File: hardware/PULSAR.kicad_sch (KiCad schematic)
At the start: 7 parts, among them J1 Conn_01x20, U1 AP2112K-3.3, U2 SS49E, U3 CD74HC4067M, U4 ADS8688

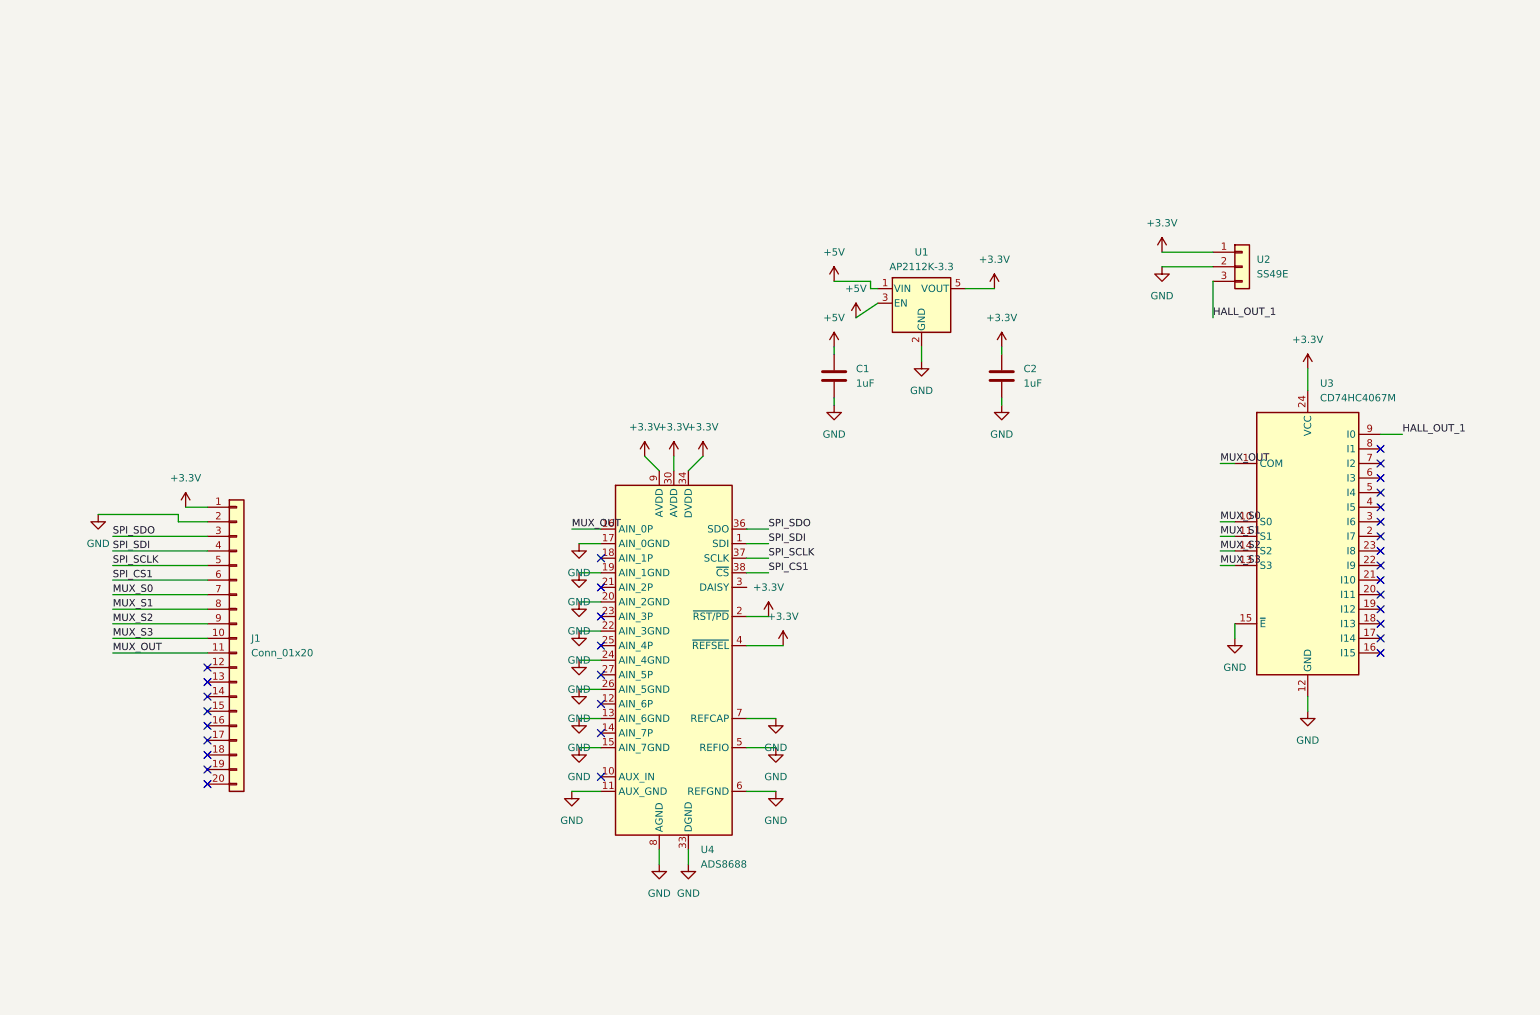
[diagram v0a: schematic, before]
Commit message: feat: add OLED SSD1306 connector with SPI signals
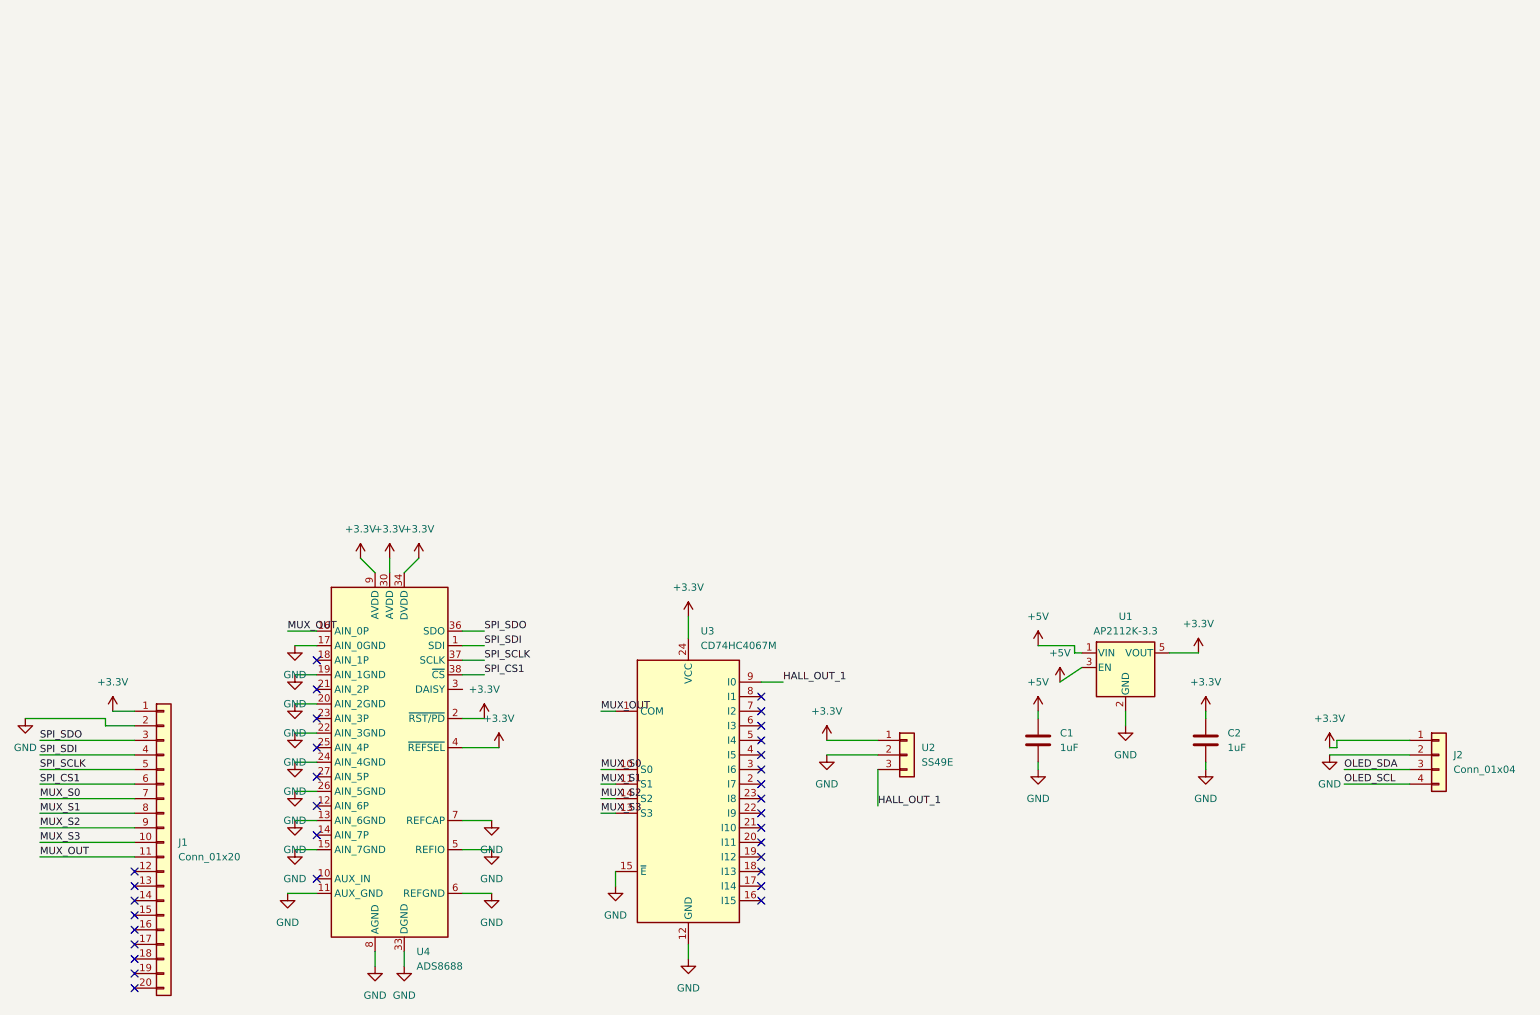
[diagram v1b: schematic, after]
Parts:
- added J2: Conn_01x04, symbol Connector_Generic:Conn_01x04
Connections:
- net +3.3V: now also J2.1 (Pin_1)
- net GND: now also J2.2 (Pin_2)
- new net OLED_SCL: J2.4 (Pin_4)
- new net OLED_SDA: J2.3 (Pin_3)
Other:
- moved on the sheet: C1, C2, J1, U1, U2, U3, U4

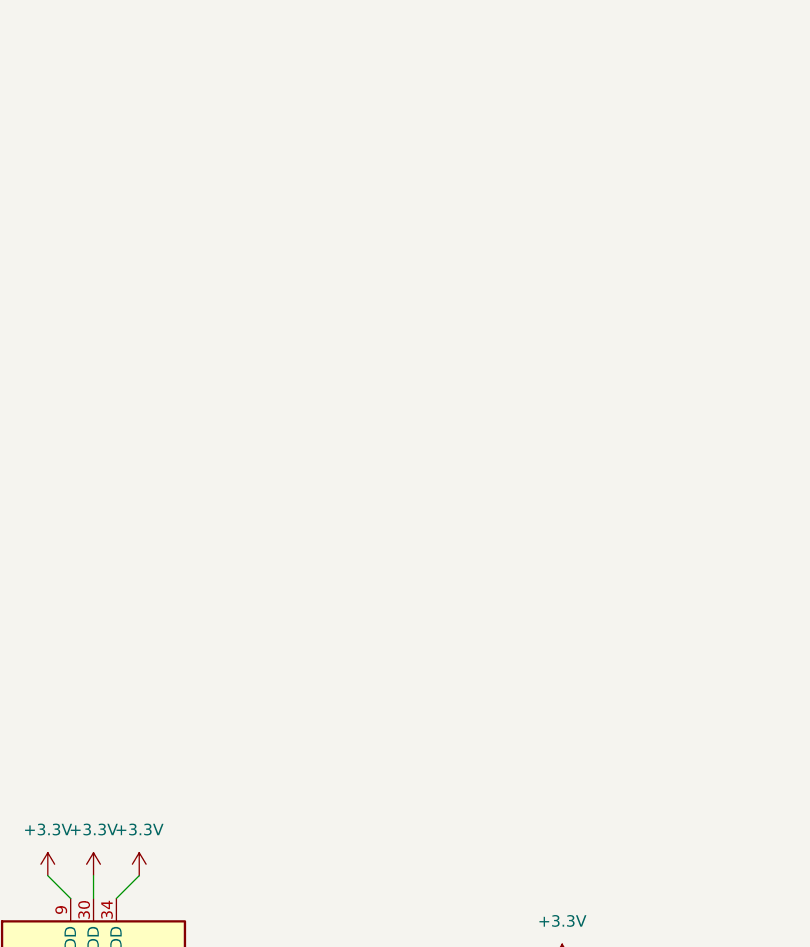
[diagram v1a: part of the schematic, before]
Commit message: feat: add USB-C connector with power and data signals
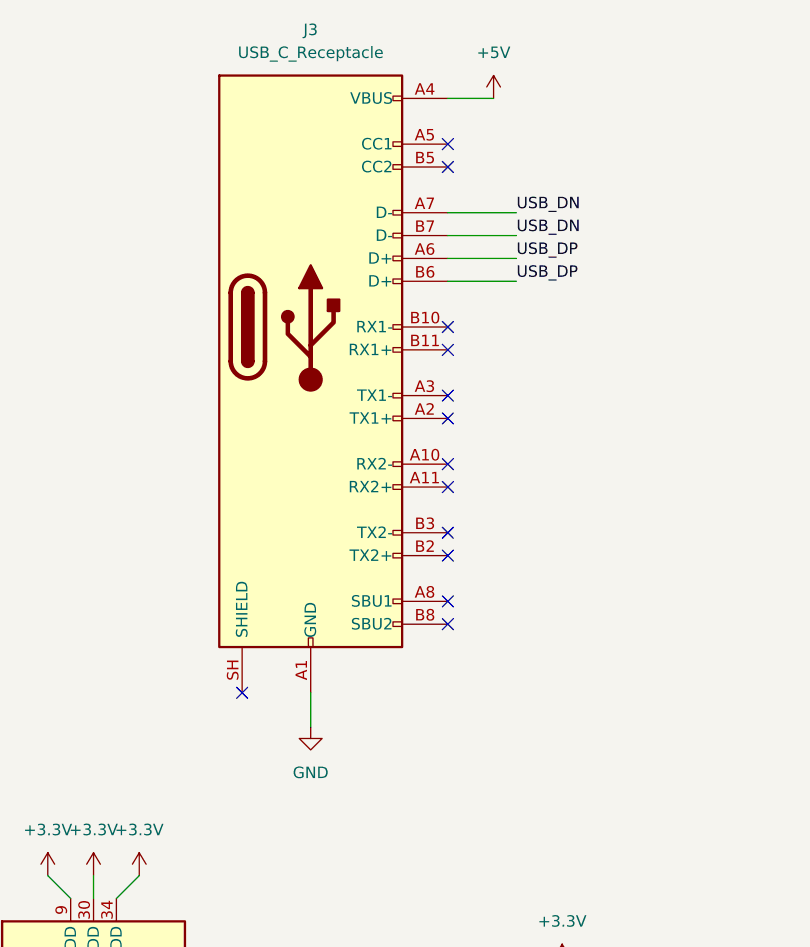
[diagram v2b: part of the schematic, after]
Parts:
- added J3: USB_C_Receptacle, symbol Connector:USB_C_Receptacle
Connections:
- net +5V: now also J3.A4 (VBUS), J3.A9 (VBUS), J3.B4 (VBUS), J3.B9 (VBUS)
- net GND: now also J3.A1 (GND), J3.A12 (GND), J3.B1 (GND), J3.B12 (GND)
- new net USB_DN: J3.A7 (D-), J3.B7 (D-)
- new net USB_DP: J3.A6 (D+), J3.B6 (D+)
- no-connect marks 32 -> 45

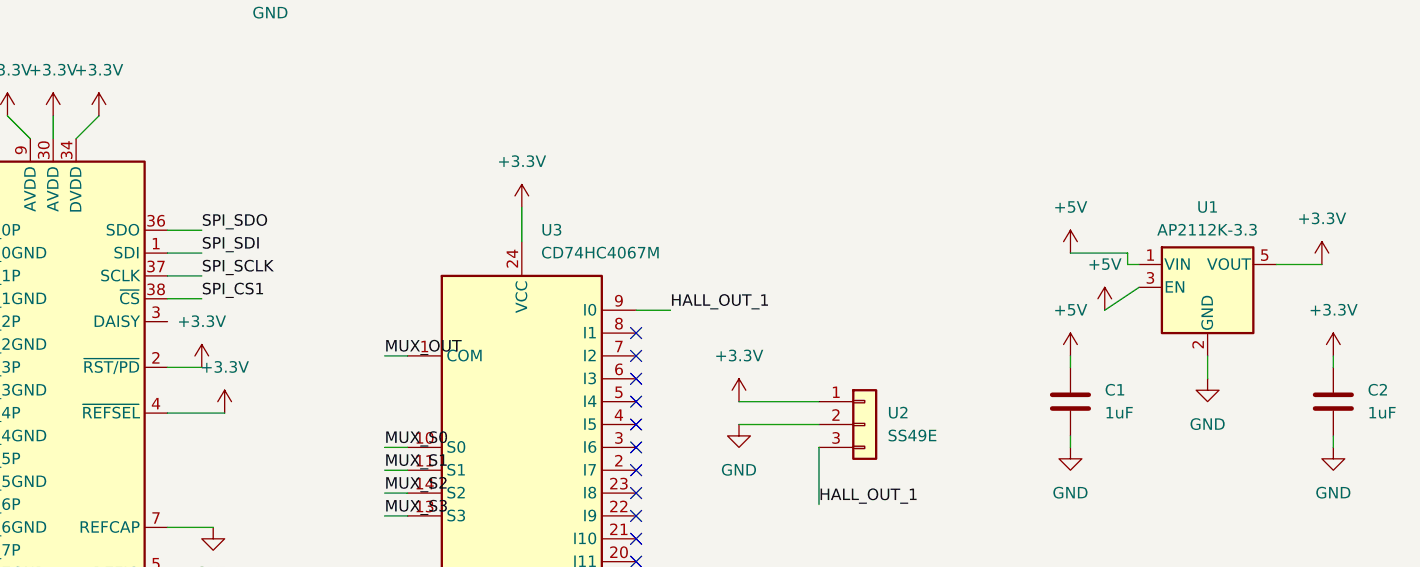
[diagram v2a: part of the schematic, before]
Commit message: fix: resolve ERC errors, add PWR_FLAG and DAISY no-connect
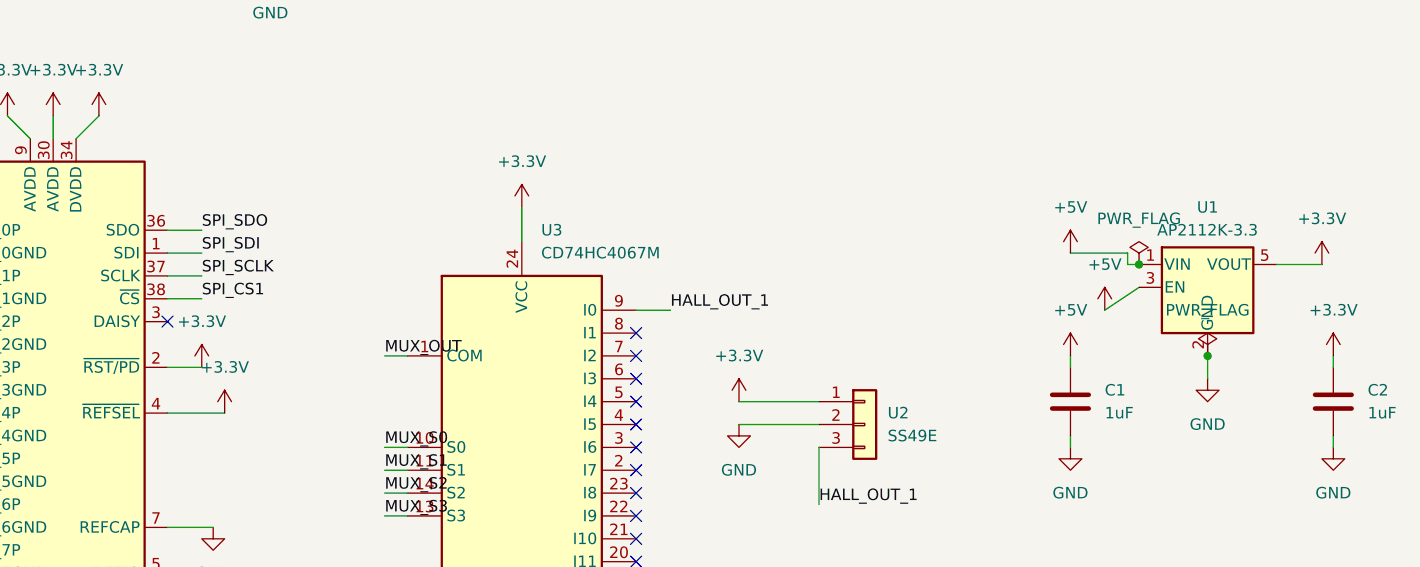
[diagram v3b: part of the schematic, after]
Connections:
- no-connect marks 45 -> 46
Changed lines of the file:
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@@
 	(generator_version "10.0")
 	(paper "A4")
+	(junction
+		(at 209.55 144.78)
+		(diameter 0)
+		(color 0 0 0 0)
+	)
+	(junction
+		(at 201.93 134.62)
+		(diameter 0)
+		(color 0 0 0 0)
+	)
 	(no_connect
 		(at 68.58 161.29)
@@
 	(no_connect
 		(at 146.05 144.78)
+	)
+	(no_connect
+		(at 93.98 140.97)
 	)
 	(no_connect
@@
 	)
 	(symbol
+		(lib_id "power:PWR_FLAG")
+		(at 209.55 144.78 0)
+		(unit 1)
+		(body_style 1)
+		(exclude_from_sim no)
+		(in_bom yes)
+		(on_board yes)
+		(in_pos_files yes)
+		(dnp no)
+		(fields_autoplaced yes)
+		(property "Reference" "#FLG02"
+			(at 209.55 142.875 0)
+			(hide yes)
+			(show_name no)
+			(do_not_autoplace no)
+			(effects
+				(font
+					(size 1.27 1.27)
+				)
+			)
+		)
+		(property "Value" "PWR_FLAG"
+			(at 209.55 139.7 0)
+			(show_name no)
+			(do_not_autoplace no)
+			(effects
+				(font
+					(size 1.27 1.27)
+				)
+			)
+		)
+		(property "Footprint" ""
+			(at 209.55 144.78 0)
+			(hide yes)
+			(show_name no)
+			(do_not_autoplace no)
+			(effects
+				(font
+					(size 1.27 1.27)
+				)
+			)
+		)
+		(property "Datasheet" ""
+			(at 209.55 144.78 0)
+			(hide yes)
+			(show_name no)
+			(do_not_autoplace no)
+			(effects
+				(font
+					(size 1.27 1.27)
+				)
+			)
+		)
+		(property "Description" "Special symbol for telling ERC where power comes from"
+			(at 209.55 144.78 0)
+			(hide yes)
+			(show_name no)
+			(do_not_autoplace no)
+			(effects
+				(font
+					(size 1.27 1.27)
+				)
+			)
+		)
+		(pin "1"
+		)
+		(instances
+			(project "PULSAR"
+				(path "/aa4da59f-af40-4eaa-aaee-8784c0a9743e"
+					(reference "#FLG02")
+					(unit 1)
+				)
+			)
+		)
+	)
+	(symbol
 		(lib_id "Connector_Generic:Conn_01x03")
 		(at 171.45 152.4 0)
@@
 					(unit 1)
 				)
+			)
+		)
+	)
+	(symbol
+		(lib_id "power:PWR_FLAG")
+		(at 201.93 134.62 0)
+		(unit 1)
+		(body_style 1)
+		(exclude_from_sim no)
+		(in_bom yes)
+		(on_board yes)
+		(in_pos_files yes)
+		(dnp no)
+		(fields_autoplaced yes)
+		(property "Reference" "#FLG01"
+			(at 201.93 132.715 0)
+			(hide yes)
+			(show_name no)
+			(do_not_autoplace no)
+			(effects
+				(font
+					(size 1.27 1.27)
+				)
+			)
+		)
+		(property "Value" "PWR_FLAG"
+			(at 201.93 129.54 0)
+			(show_name no)
+			(do_not_autoplace no)
+			(effects
+				(font
+					(size 1.27 1.27)
+				)
+			)
+		)
+		(property "Footprint" ""
+			(at 201.93 134.62 0)
+			(hide yes)
+			(show_name no)
+			(do_not_autoplace no)
+			(effects
+				(font
+					(size 1.27 1.27)
+				)
+			)
+		)
+		(property "Datasheet" ""
+			(at 201.93 134.62 0)
+			(hide yes)
+			(show_name no)
+			(do_not_autoplace no)
+			(effects
+				(font
+					(size 1.27 1.27)
+				)
+			)
+		)
+		(property "Description" "Special symbol for telling ERC where power comes from"
+			(at 201.93 134.62 0)
+			(hide yes)
+			(show_name no)
+			(do_not_autoplace no)
+			(effects
+				(font
+					(size 1.27 1.27)
+				)
+			)
+		)
+		(pin "1"
+		)
+		(instances
+			(project "PULSAR"
+				(path "/aa4da59f-af40-4eaa-aaee-8784c0a9743e"
+					(reference "#FLG01")
+					(unit 1)
+				)
